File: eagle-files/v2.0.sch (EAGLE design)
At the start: 37 parts, among them U2 MLX90614_

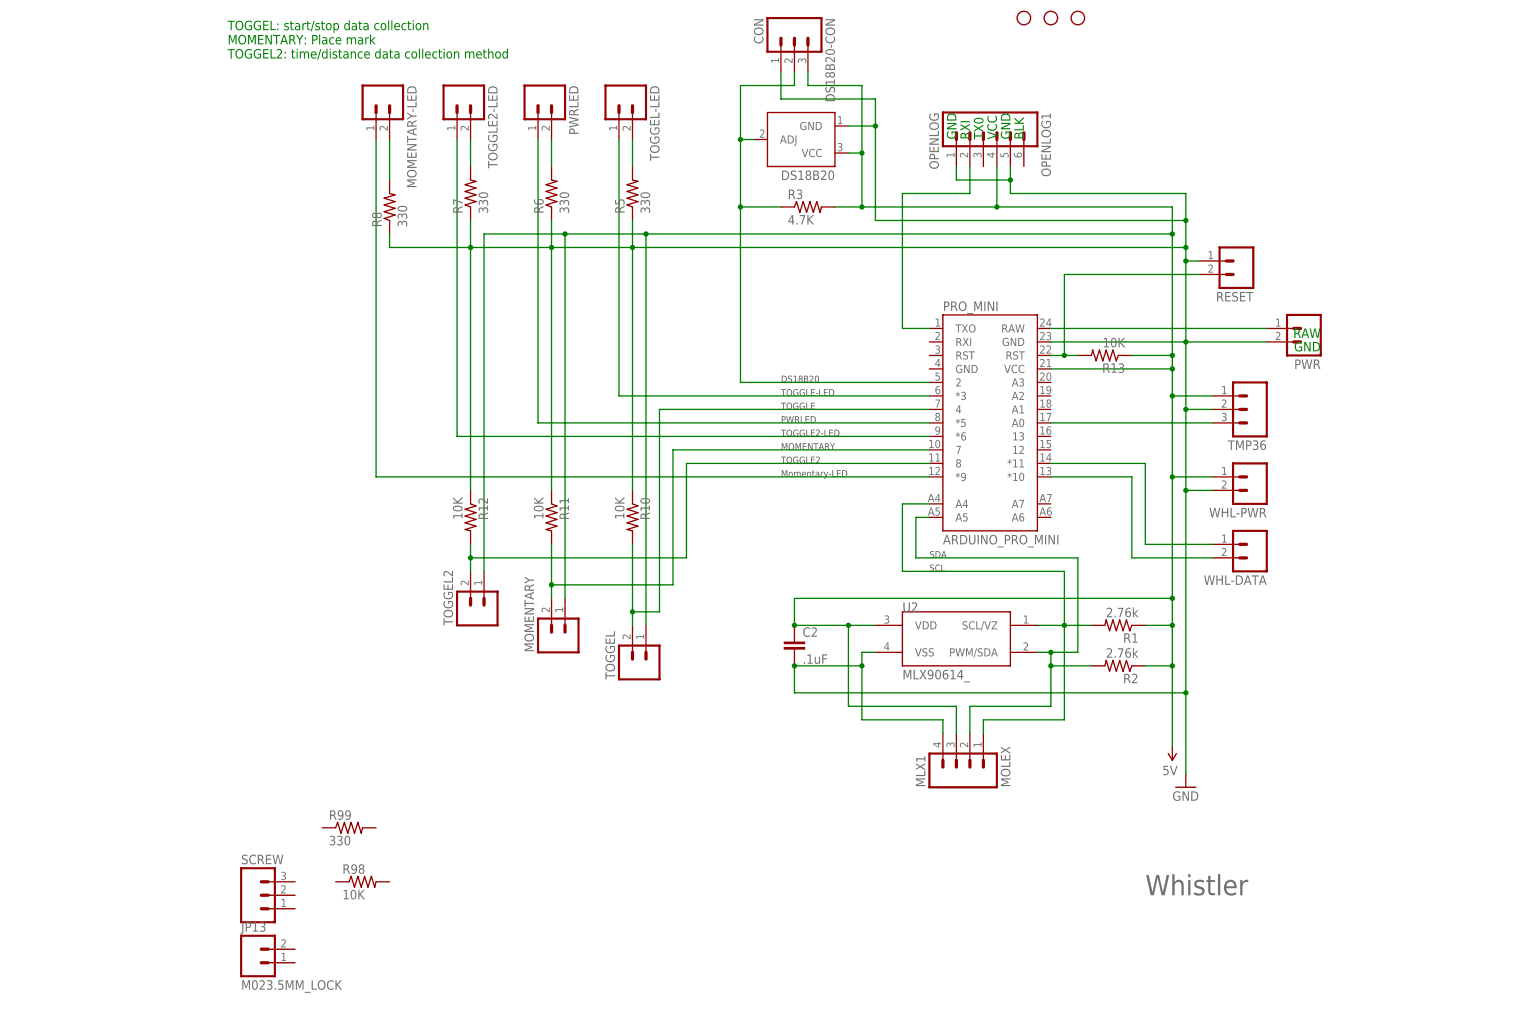
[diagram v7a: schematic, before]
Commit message: Fixed a bunch of errors with the eagle schematic. SLC and SDA were mixed up.
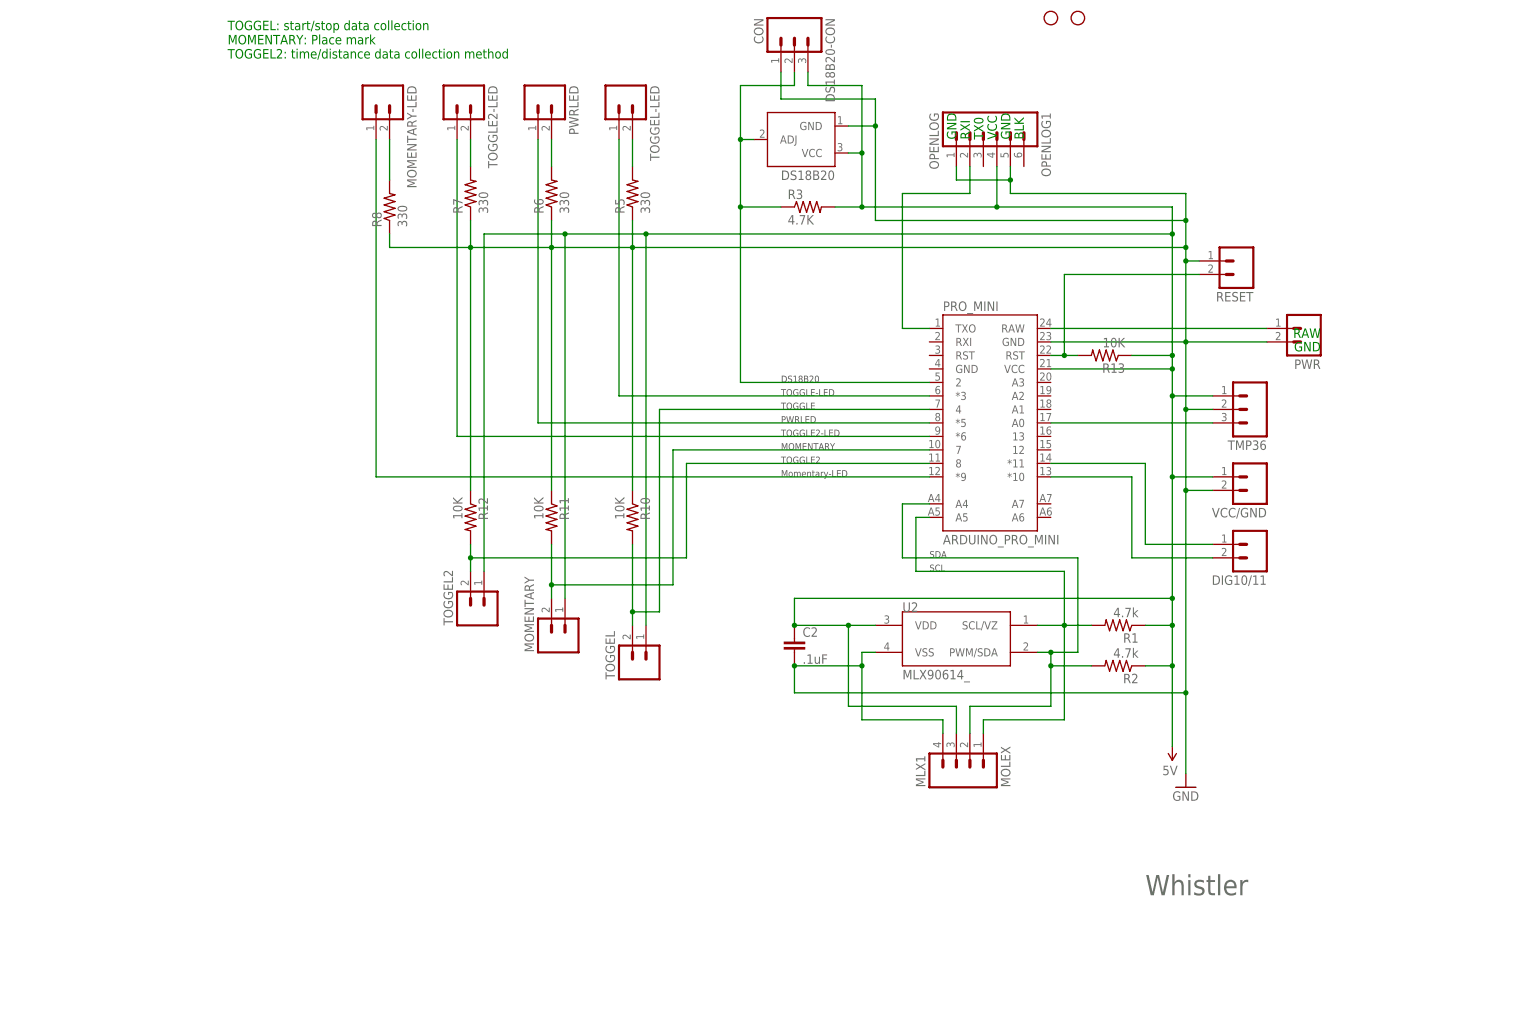
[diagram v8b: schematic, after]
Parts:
- removed JP13: M023.5MM_LOCK, SparkFun-Connectors:M023.5MM_LOCK
- removed JP8: STAND-OFFTIGHT, SparkFun:STAND-OFFTIGHT
- removed R98: 10K, SparkFun-Resistors:10KOHM1/10W1%(0603)0603
- removed R99: 330, SparkFun-Resistors:330OHM1/10W1%(0603)
- removed SCREW: (no value), SparkFun-Connectors:M03SCREW_LOCK
- R1, R2: value 2.76k -> 4.7k
- renumbered WHL-DATA to DIG10/11, WHL-PWR to VCC/GND
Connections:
- net N$21: now also PRO_MINI.A4; no longer PRO_MINI.A5
- net N$22: now also PRO_MINI.A5; no longer PRO_MINI.A4
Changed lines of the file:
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@@
 <part name="JP6" library="SparkFun" deviceset="STAND-OFF" device="TIGHT"/>
 <part name="JP7" library="SparkFun" deviceset="STAND-OFF" device="TIGHT"/>
-<part name="JP8" library="SparkFun" deviceset="STAND-OFF" device="TIGHT"/>
-<part name="SCREW" library="SparkFun-Connectors" deviceset="M03" device="SCREW_LOCK"/>
-<part name="JP13" library="SparkFun-Connectors" deviceset="M02" device="3.5MM_LOCK"/>
 <part name="TOGGEL" library="SparkFun-Connectors" deviceset="M02" device="3.5MM_LOCK" value=""/>
 <part name="DS18B20" library="SparkFun-Sensors" deviceset="TEMPERATURE-SENSOR" device="" value=""/>
@@
 <part name="PWRLED" library="SparkFun-Connectors" deviceset="M02" device="3.5MM_LOCK" value=""/>
 <part name="TOGGLE2-LED" library="SparkFun-Connectors" deviceset="M02" device="3.5MM_LOCK" value=""/>
-<part name="R99" library="SparkFun-Resistors" deviceset="330OHM1/10W1%(0603)" device="" value="330"/>
-<part name="R98" library="SparkFun-Resistors" deviceset="10KOHM1/10W1%(0603)" device="0603" value="10K"/>
 <part name="PRO_MINI" library="SparkFun-Boards" deviceset="ARDUINO_PRO_MINI" device=""/>
 <part name="PWR" library="SparkFun-Connectors" deviceset="M02" device="3.5MM_LOCK" value=""/>
 <part name="OPENLOG1" library="SparkFun" deviceset="M06" device="LOCK" value="OPENLOG"/>
 <part name="C2" library="SparkFun-Capacitors" deviceset="0.1UF-50V-20%(PTH)" device="KIT-EZ" value=".1uF"/>
-<part name="R1" library="SparkFun" deviceset="RESISTOR" device="PTH-1/4W" value="2.76k"/>
-<part name="R2" library="SparkFun" deviceset="RESISTOR" device="PTH-1/4W" value="2.76k"/>
+<part name="R1" library="SparkFun" deviceset="RESISTOR" device="PTH-1/4W" value="4.7k"/>
+<part name="R2" library="SparkFun" deviceset="RESISTOR" device="PTH-1/4W" value="4.7k"/>
 <part name="U2" library="SparkFun" deviceset="MLX90614" device="_"/>
 <part name="MLX1" library="SparkFun-Connectors" deviceset="M04" device="SMD2" value="MOLEX"/>
@@
 <part name="R11" library="SparkFun-Resistors" deviceset="10KOHM1/10W1%(0603)" device="0603" value="10K"/>
 <part name="R12" library="SparkFun-Resistors" deviceset="10KOHM1/10W1%(0603)" device="0603" value="10K"/>
-<part name="WHL-PWR" library="SparkFun-Connectors" deviceset="M02" device="3.5MM_LOCK" value=""/>
-<part name="WHL-DATA" library="SparkFun-Connectors" deviceset="M02" device="3.5MM_LOCK" value=""/>
+<part name="VCC/GND" library="SparkFun-Connectors" deviceset="M02" device="3.5MM_LOCK" value=""/>
+<part name="DIG10/11" library="SparkFun-Connectors" deviceset="M02" device="3.5MM_LOCK" value=""/>
 <part name="MOMENTARY-LED" library="SparkFun-Connectors" deviceset="M02" device="3.5MM_LOCK" value=""/>
 <part name="R8" library="SparkFun-Resistors" deviceset="330OHM1/10W1%(0603)" device="" value="330"/>
@@
 <instance part="JP6" gate="G$1" x="157.48" y="182.88"/>
 <instance part="JP7" gate="G$1" x="162.56" y="182.88"/>
-<instance part="JP8" gate="G$1" x="152.4" y="182.88"/>
-<instance part="SCREW" gate="G$1" x="7.62" y="17.78"/>
-<instance part="JP13" gate="G$1" x="7.62" y="5.08"/>
 <instance part="TOGGEL" gate="G$1" x="81.28" y="60.96" rot="R90"/>
 <instance part="DS18B20" gate="G$1" x="111.76" y="160.02" rot="R180"/>
@@
 <instance part="PWRLED" gate="G$1" x="60.96" y="167.64" rot="R270"/>
 <instance part="TOGGLE2-LED" gate="G$1" x="45.72" y="167.64" rot="R270"/>
-<instance part="R99" gate="G$1" x="25.4" y="30.48"/>
-<instance part="R98" gate="G$1" x="27.94" y="20.32"/>
 <instance part="PRO_MINI" gate="G$1" x="144.78" y="109.22"/>
 <instance part="PWR" gate="G$1" x="205.74" y="124.46" rot="R180"/>
@@
 <instance part="R11" gate="G$1" x="63.5" y="88.9" rot="R270"/>
 <instance part="R12" gate="G$1" x="48.26" y="88.9" rot="R270"/>
-<instance part="WHL-PWR" gate="G$1" x="195.58" y="96.52" rot="R180"/>
-<instance part="WHL-DATA" gate="G$1" x="195.58" y="83.82" rot="R180"/>
+<instance part="VCC/GND" gate="G$1" x="195.58" y="96.52" rot="R180"/>
+<instance part="DIG10/11" gate="G$1" x="195.58" y="83.82" rot="R180"/>
 <instance part="MOMENTARY-LED" gate="G$1" x="30.48" y="167.64" rot="R270"/>
 <instance part="R8" gate="G$1" x="33.02" y="147.32" rot="R90"/>
@@
 <wire x1="48.26" y1="93.98" x2="48.26" y2="139.7" width="0.1524" layer="91"/>
 <junction x="48.26" y="139.7"/>
-<pinref part="WHL-PWR" gate="G$1" pin="2"/>
+<pinref part="VCC/GND" gate="G$1" pin="2"/>
 <wire x1="187.96" y1="93.98" x2="182.88" y2="93.98" width="0.1524" layer="91"/>
 <junction x="182.88" y="93.98"/>
@@
 <junction x="66.04" y="142.24"/>
 <junction x="81.28" y="142.24"/>
-<pinref part="WHL-PWR" gate="G$1" pin="1"/>
+<pinref part="VCC/GND" gate="G$1" pin="1"/>
 <wire x1="187.96" y1="96.52" x2="180.34" y2="96.52" width="0.1524" layer="91"/>
 <junction x="180.34" y="96.52"/>
@@
 <net name="N$3" class="0">
 <segment>
-<pinref part="WHL-DATA" gate="G$1" pin="1"/>
+<pinref part="DIG10/11" gate="G$1" pin="1"/>
 <wire x1="175.26" y1="83.82" x2="187.96" y2="83.82" width="0.1524" layer="91"/>
 <pinref part="PRO_MINI" gate="G$1" pin="*11"/>
@@
 <net name="N$11" class="0">
 <segment>
-<pinref part="WHL-DATA" gate="G$1" pin="2"/>
+<pinref part="DIG10/11" gate="G$1" pin="2"/>
 <wire x1="187.96" y1="81.28" x2="172.72" y2="81.28" width="0.1524" layer="91"/>
 <pinref part="PRO_MINI" gate="G$1" pin="*10"/>
@@
 <wire x1="157.48" y1="63.5" x2="162.56" y2="63.5" width="0.1524" layer="91"/>
 <wire x1="162.56" y1="63.5" x2="162.56" y2="81.28" width="0.1524" layer="91"/>
-<wire x1="162.56" y1="81.28" x2="132.08" y2="81.28" width="0.1524" layer="91"/>
-<pinref part="PRO_MINI" gate="G$1" pin="A5"/>
-<wire x1="132.08" y1="81.28" x2="132.08" y2="88.9" width="0.1524" layer="91"/>
-<wire x1="132.08" y1="88.9" x2="134.62" y2="88.9" width="0.1524" layer="91"/>
 <junction x="157.48" y="63.5"/>
 <pinref part="R2" gate="G$1" pin="2"/>
@@
 <wire x1="157.48" y1="53.34" x2="157.48" y2="60.96" width="0.1524" layer="91"/>
 <junction x="157.48" y="60.96"/>
+<wire x1="162.56" y1="81.28" x2="129.54" y2="81.28" width="0.1524" layer="91"/>
+<wire x1="129.54" y1="81.28" x2="129.54" y2="91.44" width="0.1524" layer="91"/>
+<pinref part="PRO_MINI" gate="G$1" pin="A4"/>
+<wire x1="129.54" y1="91.44" x2="134.62" y2="91.44" width="0.1524" layer="91"/>
 </segment>
 </net>
@@
 <wire x1="160.02" y1="68.58" x2="154.94" y2="68.58" width="0.1524" layer="91"/>
 <wire x1="160.02" y1="68.58" x2="160.02" y2="78.74" width="0.1524" layer="91"/>
-<wire x1="160.02" y1="78.74" x2="129.54" y2="78.74" width="0.1524" layer="91"/>
-<pinref part="PRO_MINI" gate="G$1" pin="A4"/>
-<wire x1="129.54" y1="78.74" x2="129.54" y2="91.44" width="0.1524" layer="91"/>
-<wire x1="129.54" y1="91.44" x2="134.62" y2="91.44" width="0.1524" layer="91"/>
+<wire x1="160.02" y1="78.74" x2="132.08" y2="78.74" width="0.1524" layer="91"/>
 <junction x="160.02" y="68.58"/>
 <pinref part="R1" gate="G$1" pin="2"/>
 <wire x1="165.1" y1="68.58" x2="160.02" y2="68.58" width="0.1524" layer="91"/>
 <wire x1="160.02" y1="50.8" x2="160.02" y2="68.58" width="0.1524" layer="91"/>
-</segment>
-</net>
+<pinref part="PRO_MINI" gate="G$1" pin="A5"/>
+<wire x1="132.08" y1="78.74" x2="132.08" y2="88.9" width="0.1524" layer="91"/>
+<wire x1="132.08" y1="88.9" x2="134.62" y2="88.9" width="0.1524" layer="91"/>
+</segment>
+</net>
